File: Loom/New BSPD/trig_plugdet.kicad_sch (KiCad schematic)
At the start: 18 parts, among them U1 MCP6542, U3 4011, U4 4011, U5 MCP6542

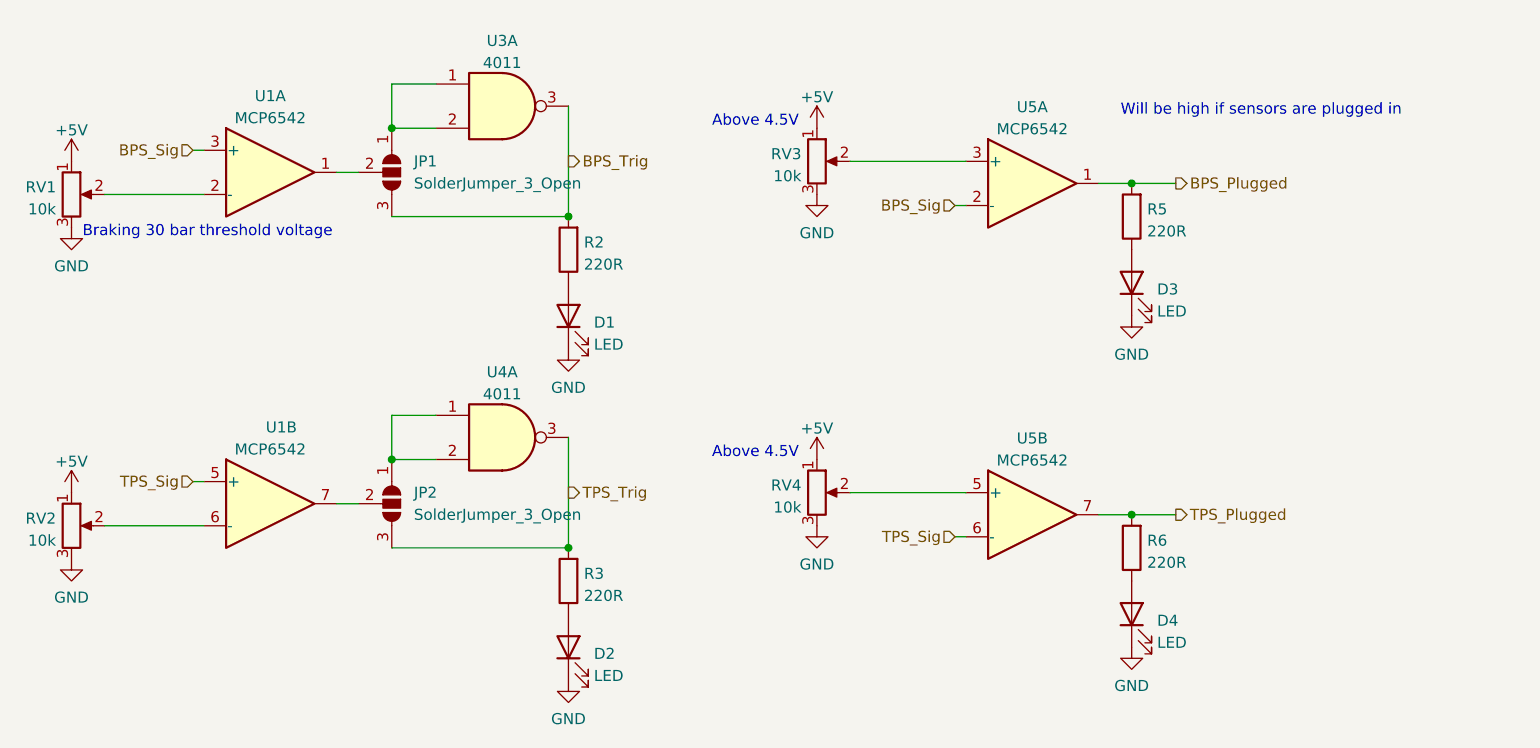
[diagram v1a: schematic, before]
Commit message: Complete BSPD Schematic
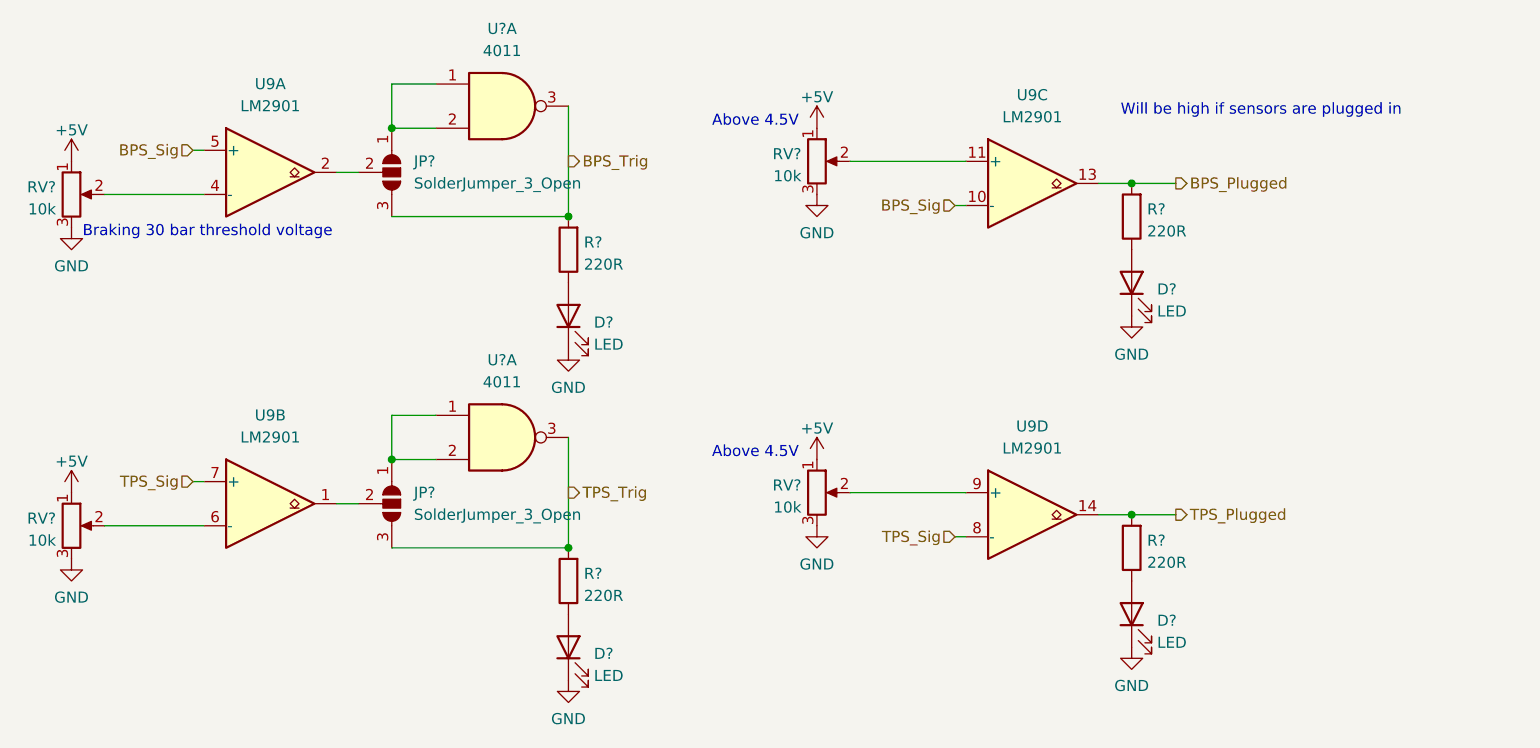
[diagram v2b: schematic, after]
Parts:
- removed U1, U5: MCP6542, Package_DIP:DIP-8_W7.62mm_LongPads, symbol Additional_Components:MCP6542
- added U9: LM2901, symbol Comparator:LM2901
- U?: renamed from U3; footprint Package_DIP:DIP-14_W7.62mm_LongPads -> (none)
- U?: renamed from U4; footprint Package_DIP:DIP-14_W7.62mm_LongPads -> (none)
- renumbered D4 to D?, D2 to D?, D3 to D?, D1 to D?, JP2 to JP?, JP1 to JP?, R2 to R?, R3 to R?, R5 to R?, R6 to R?, RV4 to RV?, RV3 to RV?, RV2 to RV?, RV1 to RV?
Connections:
- net BPS_Plugged: now also U9.13
- net BPS_Sig: now also U9.10 (-), U9.5 (+)
- net TPS_Plugged: now also U9.14
- net TPS_Sig: now also U9.7 (+), U9.8 (-)
- net at JP?.2 (C): now also U9.1
- net at RV?.2: now also U9.9 (+)
- net at JP?.2 (C): now also U9.2
- net at RV?.2: now also U9.11 (+)
- net at RV?.2: now also U9.6 (-)
- net at RV?.2: now also U9.4 (-)

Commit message: Complete Schematic, Footprint Assignment, Start PCB Design
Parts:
- JP? (x2): footprint (none) -> Jumper:SolderJumper-3_P1.3mm_Open_RoundedPad1.0x1.5mm
- U9, U? (x2): footprint (none) -> Package_DIP:DIP-14_W7.62mm_Socket
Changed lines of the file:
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@@
       (effects (font (size 1.27 1.27)) (justify left))
     )
-    (property "Footprint" "" (at 67.31 74.93 0)
+    (property "Footprint" "Jumper:SolderJumper-3_P1.3mm_Open_RoundedPad1.0x1.5mm" (at 67.31 74.93 0)
       (effects (font (size 1.27 1.27)) hide)
     )
@@
       (effects (font (size 1.27 1.27)) (justify left))
     )
-    (property "Footprint" "" (at 67.31 36.83 0)
+    (property "Footprint" "Jumper:SolderJumper-3_P1.3mm_Open_RoundedPad1.0x1.5mm" (at 67.31 36.83 0)
       (effects (font (size 1.27 1.27)) hide)
     )
@@
       (effects (font (size 1.27 1.27)))
     )
-    (property "Footprint" "" (at 80.01 29.21 0)
+    (property "Footprint" "Package_DIP:DIP-14_W7.62mm_Socket" (at 80.01 29.21 0)
       (effects (font (size 1.27 1.27)) hide)
     )
@@
       (effects (font (size 1.27 1.27)))
     )
-    (property "Footprint" "" (at 139.7 35.56 0)
+    (property "Footprint" "Package_DIP:DIP-14_W7.62mm_Socket" (at 139.7 35.56 0)
       (effects (font (size 1.27 1.27)) hide)
     )
@@
       (effects (font (size 1.27 1.27)))
     )
-    (property "Footprint" "" (at 139.7 73.66 0)
+    (property "Footprint" "Package_DIP:DIP-14_W7.62mm_Socket" (at 139.7 73.66 0)
       (effects (font (size 1.27 1.27)) hide)
     )
@@
       (effects (font (size 1.27 1.27)))
     )
-    (property "Footprint" "" (at 52.07 34.29 0)
+    (property "Footprint" "Package_DIP:DIP-14_W7.62mm_Socket" (at 52.07 34.29 0)
       (effects (font (size 1.27 1.27)) hide)
     )
@@
       (effects (font (size 1.27 1.27)))
     )
-    (property "Footprint" "" (at 52.07 72.39 0)
+    (property "Footprint" "Package_DIP:DIP-14_W7.62mm_Socket" (at 52.07 72.39 0)
       (effects (font (size 1.27 1.27)) hide)
     )
@@
       (effects (font (size 1.27 1.27)))
     )
-    (property "Footprint" "" (at 80.01 67.31 0)
-      (effects (font (size 1.27 1.27)) hide)
-    )
+    (property "Footprint" "Package_DIP:DIP-14_W7.62mm_Socket" (at 80.01 67.31 0)
+      (effects (font (size 1.27 1.27)) hide)
+    )

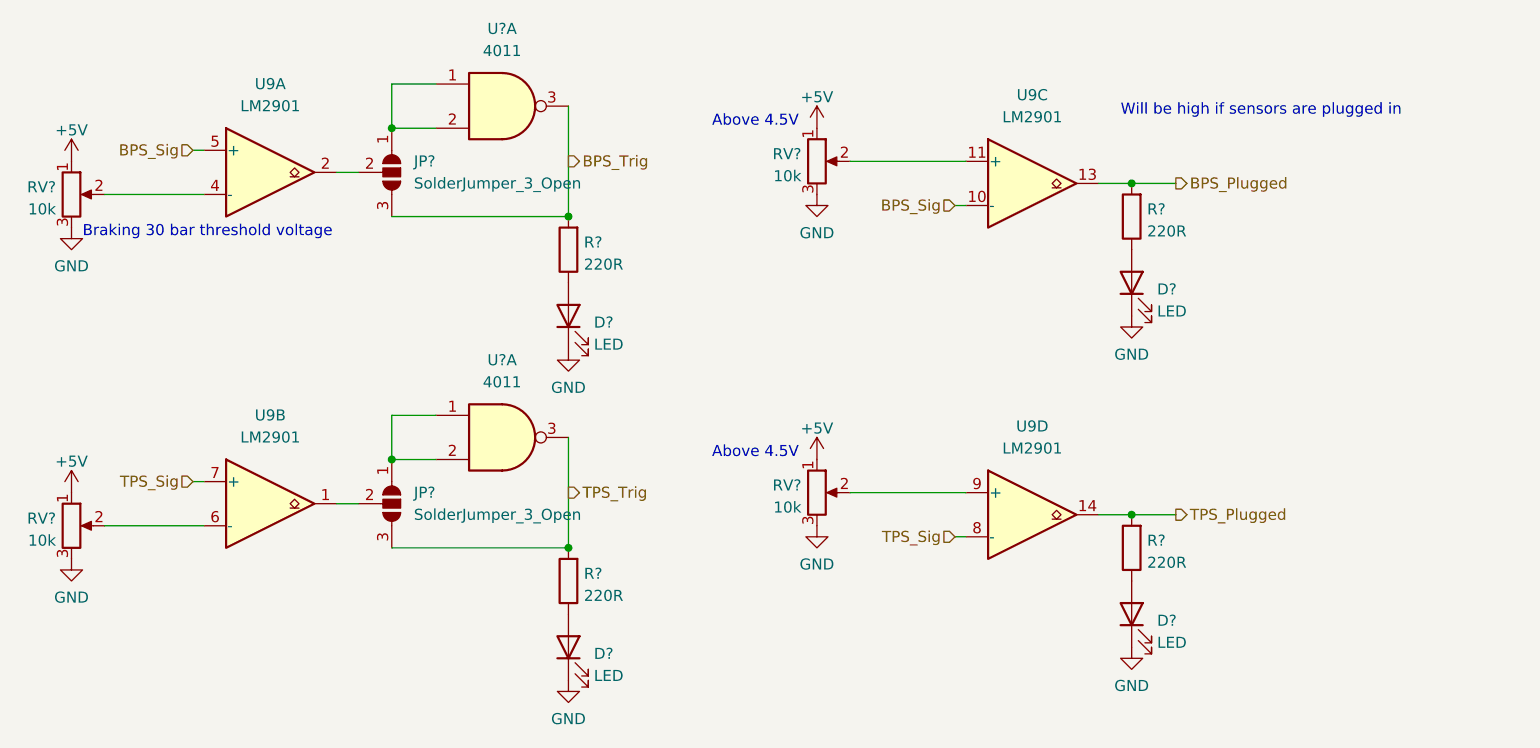
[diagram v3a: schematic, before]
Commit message: Fix BSPD Crystal Footprint
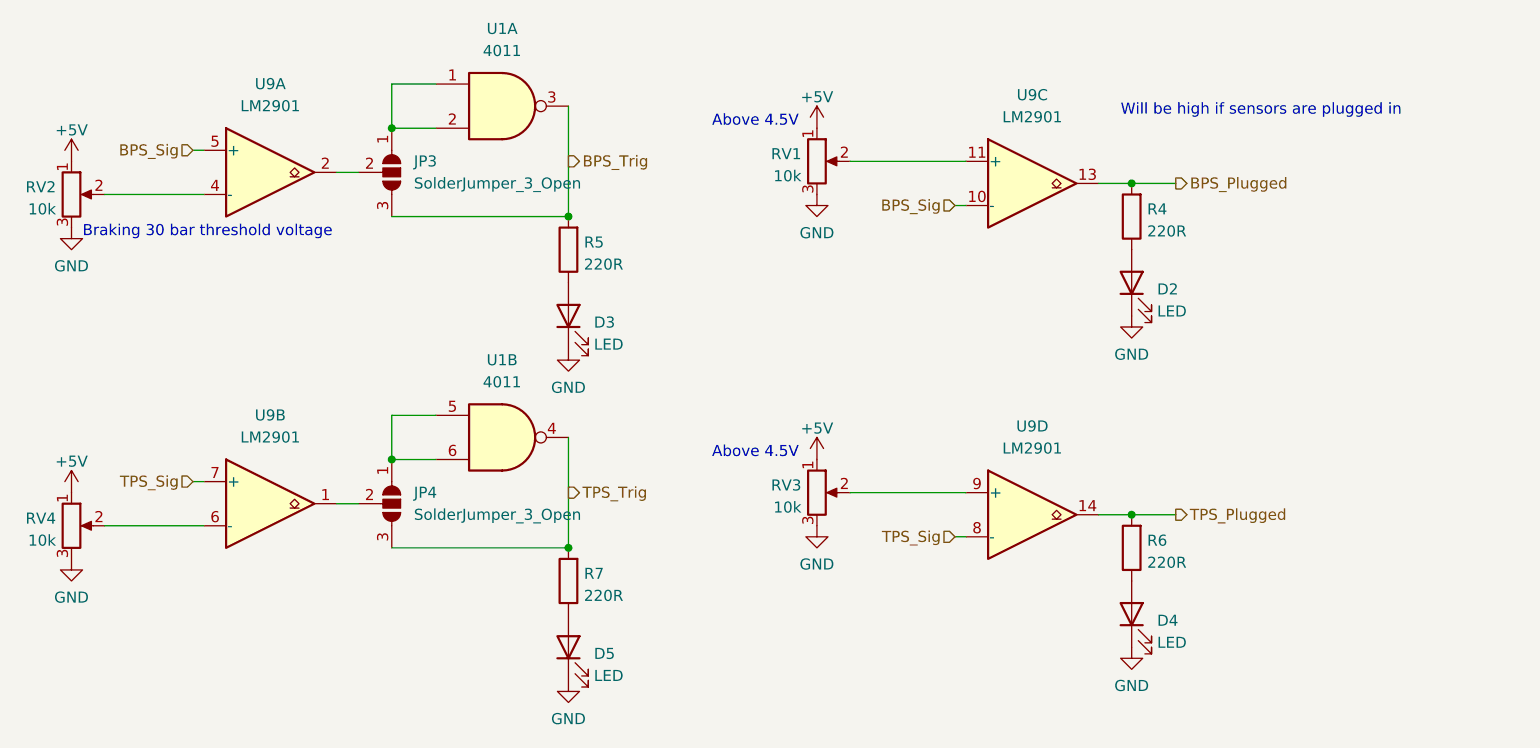
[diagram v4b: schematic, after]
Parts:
- gave numbers to parts that had none: 15
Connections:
- net TPS_Trig: now also U1.4; no longer U1.3
- new net: JP4.1 (A), U1.5, U1.6
